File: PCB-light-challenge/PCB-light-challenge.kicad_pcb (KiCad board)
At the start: 2 copper layers, 79.9 x 79 mm, 39 parts, among them J1 Screw_Terminal_01x03, J2 Conn_01x04_Socket, J3 Conn_01x18_Socket, J4 Conn_01x12_Socket, U2 AP9101CK, U3 SP8K32FRATB

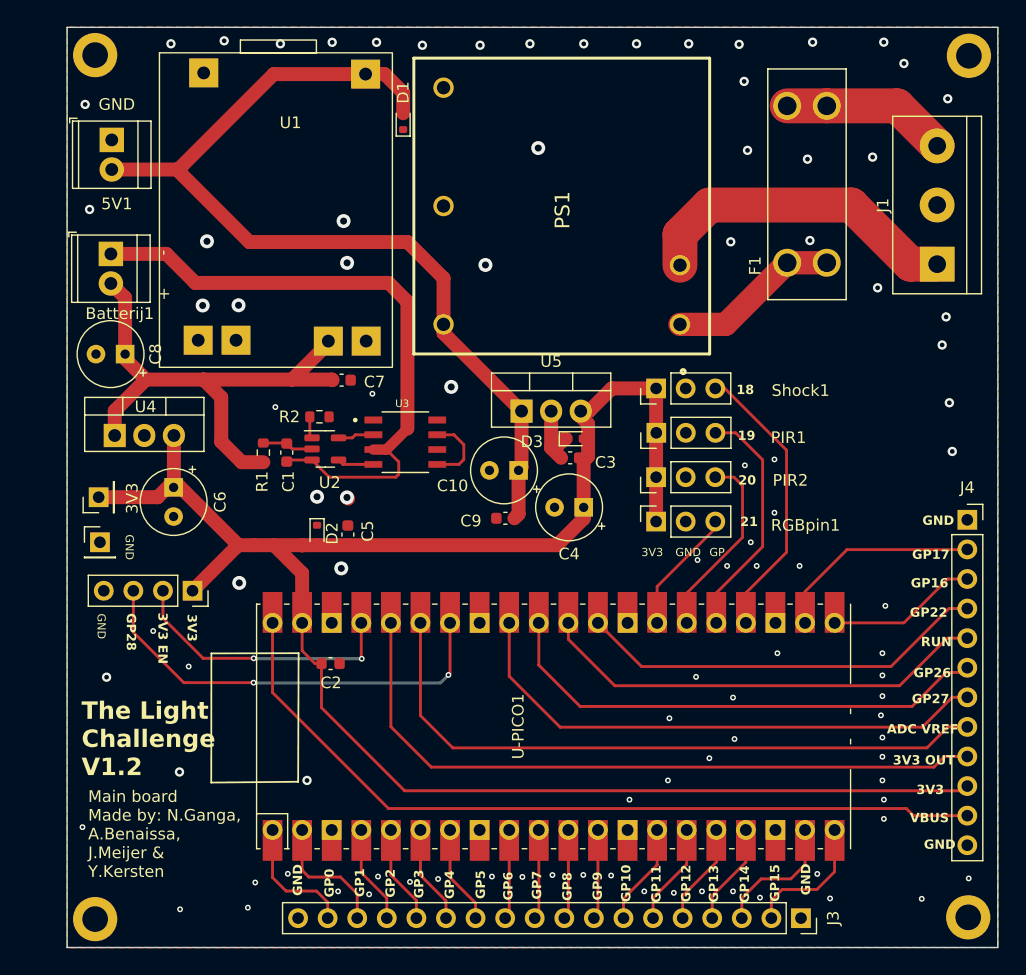
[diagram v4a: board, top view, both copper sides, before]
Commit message: 3V3 OUT voor RGB toegevoegd en footprint van connectoren verandert naar JST
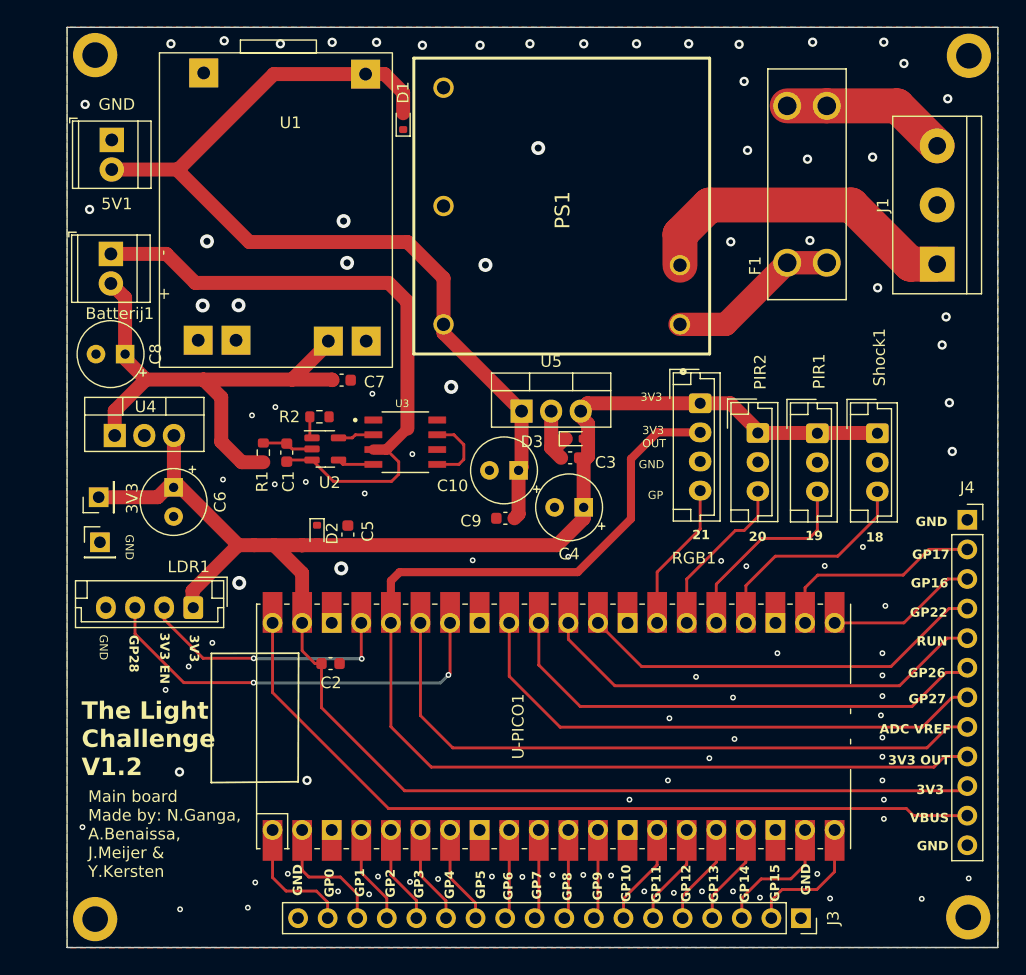
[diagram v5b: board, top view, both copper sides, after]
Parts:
- removed RGBpin1: Conn_01x03_Socket, Connector_PinSocket_2.54mm:PinSocket_1x03_P2.54mm_Vertical
- added RGB1: RGB, Connector_JST:JST_EH_B4B-EH-A_1x04_P2.50mm_Vertical, F.Cu at (226.8, 105.4)
- LDR1: renamed from J2; value Conn_01x04_Socket -> LDR; footprint Connector_PinSocket_2.54mm:PinSocket_1x04_P2.54mm_Vertical -> Connector_JST:JST_EH_B4B-EH-A_1x04_P2.50mm_Vertical
- PIR1, PIR2, Shock1: footprint Connector_PinHeader_2.54mm:PinHeader_1x03_P2.54mm_Vertical -> Connector_JST:JST_EH_B3B-EH-A_1x03_P2.50mm_Vertical
- moved Shock1 19.4 mm to (242.0, 108.0), turned to -90 degrees
- moved PIR1 13.8 mm to (236.9, 108.0), turned to -90 degrees
- moved PIR2 9.53 mm to (231.7, 108.0), turned to -90 degrees
- moved LDR1 1.45 mm to (183.3, 123.0), turned to 180 degrees
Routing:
- net 3V3 OUT: track 60.2 -> 98.7 mm
- net 3V3: track 159.1 -> 168.9 mm
- net GP18: track 24.6 -> 19.1 mm
- net GP19: track 20.7 -> 17.2 mm
- net GP20: track 16.4 -> 14.3 mm
- net GP21: track 10.8 -> 12.9 mm
- net GP28: track 37.2 -> 35.7 mm
- net 3V3 EN: track 24.1 -> 22.6 mm
- net P-: track 6.48 -> 6.34 mm, vias 98 -> 100

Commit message: LDR connector, silkscreen AC,  Mounting hole main pcb aangepast
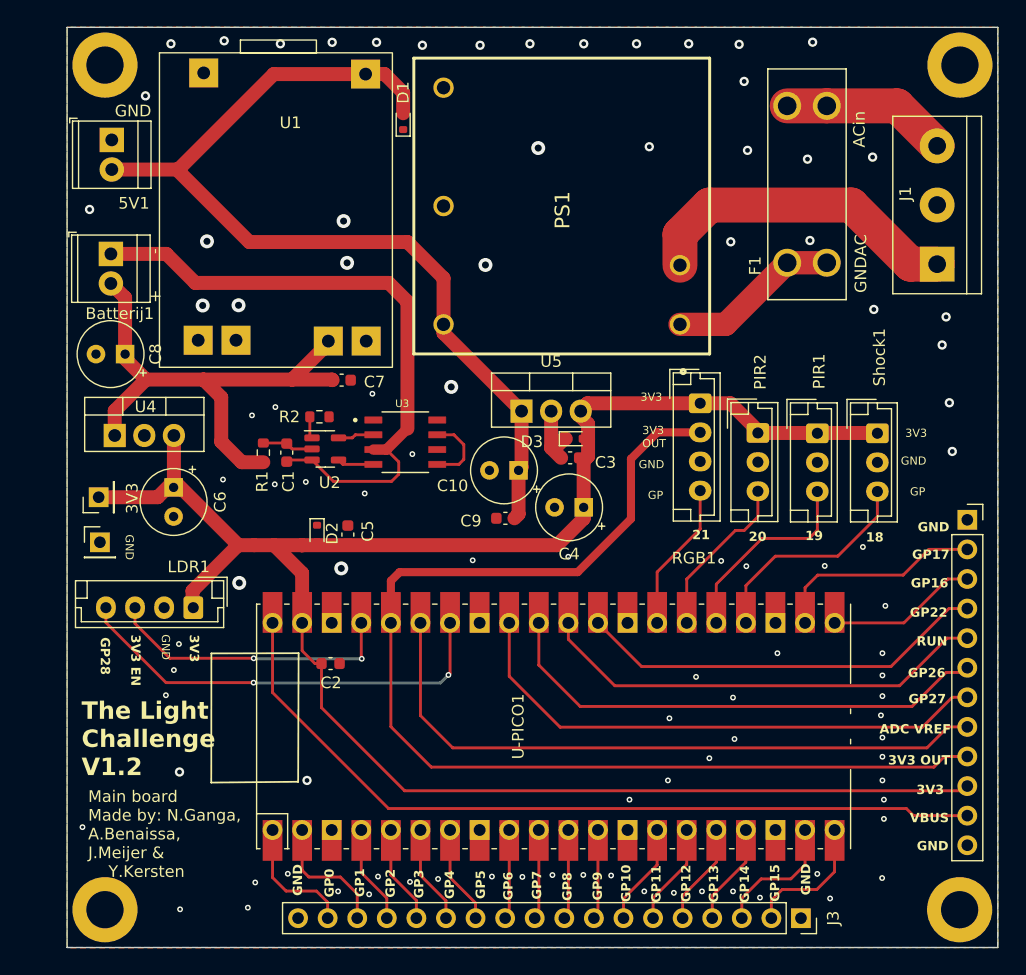
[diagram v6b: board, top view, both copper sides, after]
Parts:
- H1, H2, H3, H4: footprint MountingHole:MountingHole_2.2mm_M2_DIN965_Pad -> MountingHole:MountingHole_3.2mm_M3_DIN965_Pad
- moved H2 1.20 mm to (175.7, 76.4)
- moved H1 1.16 mm to (175.7, 148.9)
- moved H3 1.11 mm to (249.1, 76.4)
- moved H4 0.99 mm to (249.1, 148.9)
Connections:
- LDR1 pad 2: 3V3 EN -> P-
- LDR1 pad 3: GP28 -> 3V3 EN
- LDR1 pad 4: P- -> GP28
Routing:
- net 3V3 EN: track 22.6 -> 25.3 mm
- net GP28: track 35.7 -> 37.6 mm
- net P-: vias 100 -> 97
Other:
- board text added: "ACin"
- board text added: "GNDAC"

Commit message: AC (L) en (N)  weer nagekeken en aangepast
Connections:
- PS1 pad 1: /Battery_charger/Fuse -> /Battery_charger/GNDAC
- PS1 pad 2: /Battery_charger/GNDAC -> /Battery_charger/Fuse
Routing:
- net /Battery_charger/GNDAC: track 27.9 -> 25.1 mm
- net /Battery_charger/Fuse: track 14.8 -> 12.7 mm
- net P-: vias 97 -> 96
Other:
- board text added: "AC(L)"
- board text added: "AC(N)"
- board text removed: "ACin"
- board text removed: "GNDAC"
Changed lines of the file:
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@@
       (stroke (width 0.254) (type solid)) (layer "F.Fab"))
     (pad "1" thru_hole circle (at -10.16 10.15 90) (size 1.75 1.75) (drill 1.15) (layers "*.Cu" "*.Mask")
-      (net 41 "/Battery_charger/Fuse") (pinfunction "AC(N)") (pintype "passive"))
+      (net 43 "/Battery_charger/GNDAC") (pinfunction "AC(N)") (pintype "passive"))
     (pad "2" thru_hole circle (at -5.08 10.15 90) (size 1.75 1.75) (drill 1.15) (layers "*.Cu" "*.Mask")
-      (net 43 "/Battery_charger/GNDAC") (pinfunction "AC(L)") (pintype "passive"))
+      (net 41 "/Battery_charger/Fuse") (pinfunction "AC(L)") (pintype "passive"))
     (pad "3" thru_hole circle (at 10.16 -10.15 90) (size 1.75 1.75) (drill 1.15) (layers "*.Cu" "*.Mask")
       (net 42 "unconnected-(PS1-NC-Pad3)") (pinfunction "NC") (pintype "no_connect"))
@@
     (effects (font (size 0.8 0.8) (thickness 0.15) bold) (justify left bottom))
   )
-  (gr_text "GNDAC" (at 240.5888 93.4212 90) (layer "F.SilkS")
+  (gr_text "AC(N)" (at 240.5888 93.4212 90) (layer "F.SilkS")
     (effects (font (size 1 1) (thickness 0.15)))
   )
-  (gr_text "ACin" (at 240.4618 81.8896 90) (layer "F.SilkS")
+  (gr_text "AC(L)" (at 240.4618 81.8896 90) (layer "F.SilkS")
     (effects (font (size 1 1) (thickness 0.15)))
   )
@@
   (segment (start 206.502 108.966) (end 206.502 110.236) (width 0.25) (layer "F.Cu") (net 39))
   (segment (start 234.266 79.879) (end 237.666 79.879) (width 3) (layer "F.Cu") (net 40))
-  (segment (start 237.666 79.879) (end 243.709 79.879) (width 3) (layer "F.Cu") (net 40))
-  (segment (start 243.709 79.879) (end 247.142 83.312) (width 3) (layer "F.Cu") (net 40))
-  (segment (start 225.06 98.64) (end 228.975 98.64) (width 2) (layer "F.Cu") (net 41))
-  (segment (start 234.266 93.349) (end 237.666 93.349) (width 2) (layer "F.Cu") (net 41))
-  (segment (start 228.975 98.64) (end 234.266 93.349) (width 2) (layer "F.Cu") (net 41))
-  (segment (start 225.06 90.916) (end 225.06 93.56) (width 3) (layer "F.Cu") (net 43))
-  (segment (start 244.856 93.472) (end 239.776 88.392) (width 3) (layer "F.Cu") (net 43))
-  (segment (start 239.776 88.392) (end 227.584 88.392) (width 3) (layer "F.Cu") (net 43))
-  (segment (start 247.142 93.472) (end 244.856 93.472) (width 3) (layer "F.Cu") (net 43))
-  (segment (start 227.584 88.392) (end 225.06 90.916) (width 3) (layer "F.Cu") (net 43))
+  (segment (start 247.142 83.312) (end 243.709 79.879) (width 3) (layer "F.Cu") (net 40))
+  (segment (start 243.709 79.879) (end 237.666 79.879) (width 3) (layer "F.Cu") (net 40))
+  (segment (start 237.666 93.349) (end 234.266 93.349) (width 2) (layer "F.Cu") (net 41))
+  (segment (start 234.055 93.56) (end 234.266 93.349) (width 2) (layer "F.Cu") (net 41))
+  (segment (start 225.06 93.56) (end 234.055 93.56) (width 2) (layer "F.Cu") (net 41))
+  (segment (start 247.142 93.472) (end 240.919 99.695) (width 3) (layer "F.Cu") (net 43))
+  (segment (start 240.919 99.695) (end 226.115 99.695) (width 3) (layer "F.Cu") (net 43))
+  (segment (start 226.115 99.695) (end 225.06 98.64) (width 3) (layer "F.Cu") (net 43))
   (segment (start 214 109.242) (end 214.858 110.1) (width 1.2) (layer "F.Cu") (net 44))
   (segment (start 214 106.09) (end 214 109.242) (width 1.2) (layer "F.Cu") (net 44))
@@
   (via (at 224.155 132.461) (size 0.5) (drill 0.25) (layers "F.Cu" "B.Cu") (free) (net 44))
   (via (at 242.443 134.112) (size 0.5) (drill 0.25) (layers "F.Cu" "B.Cu") (free) (net 44))
-  (via (at 241.7064 97.3582) (size 0.8) (drill 0.4) (layers "F.Cu" "B.Cu") (free) (net 44))
   (via (at 247.91 98) (size 0.8) (drill 0.4) (layers "F.Cu" "B.Cu") (free) (net 44))
   (via (at 236.22 91.44) (size 0.8) (drill 0.4) (layers "F.Cu" "B.Cu") (free) (net 44))

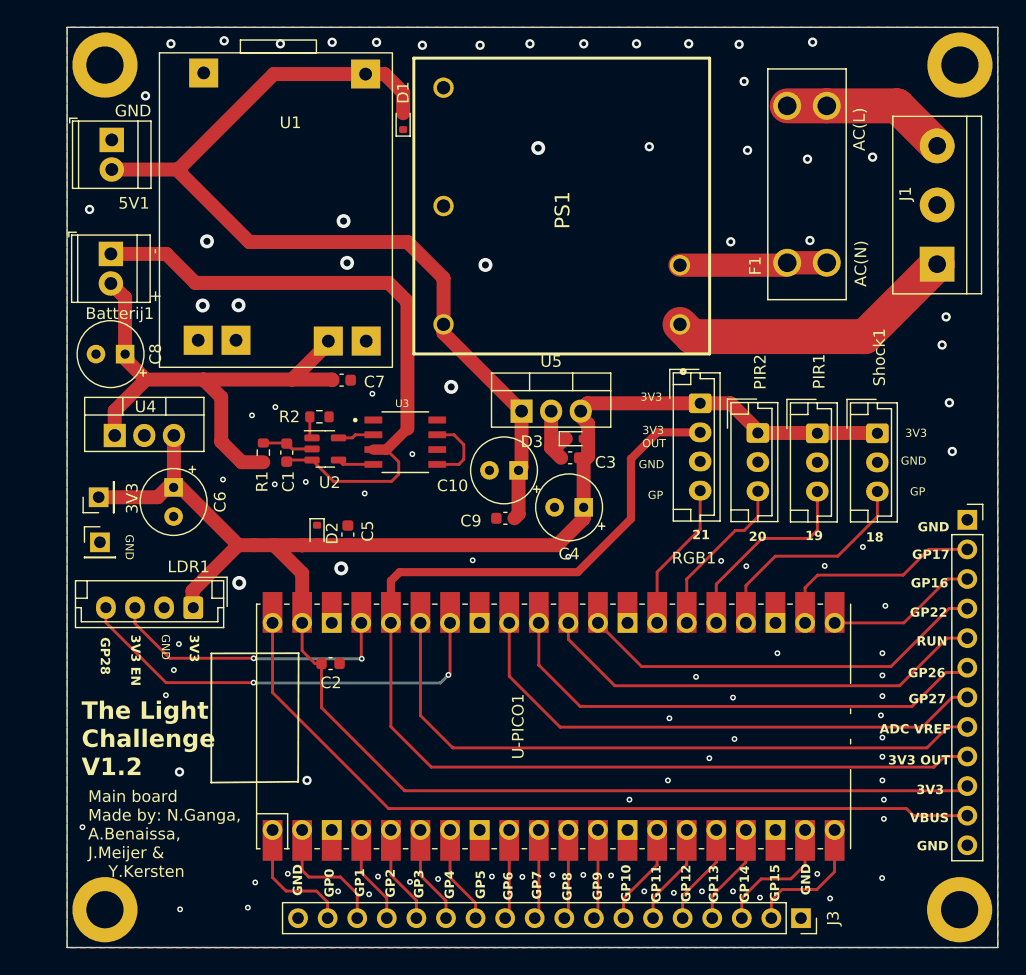
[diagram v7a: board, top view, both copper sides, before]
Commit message: Footprint charger aangepast, connectoren verder van elkaar geplaatst.
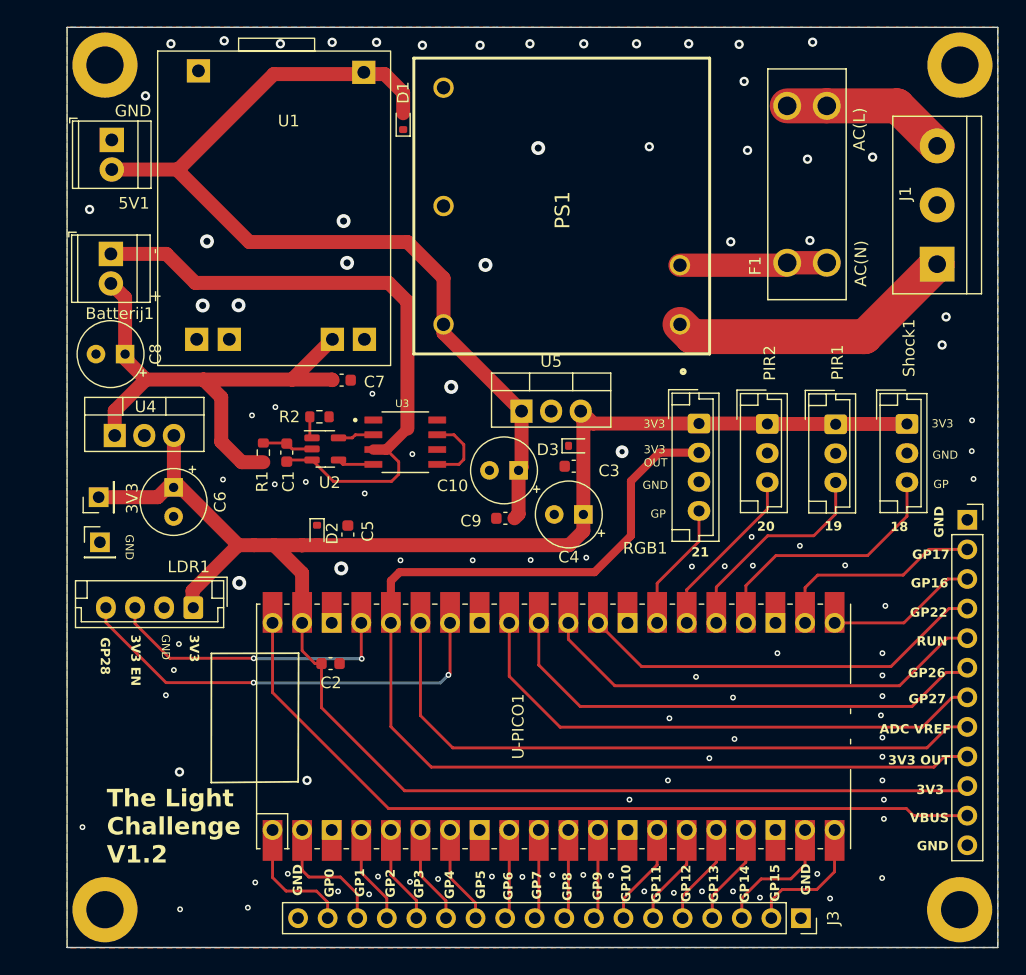
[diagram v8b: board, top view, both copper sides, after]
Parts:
- moved Shock1 2.66 mm to (244.6, 107.2)
- moved PIR1 1.75 mm to (238.4, 107.2)
- moved RGB1 1.74 mm to (226.7, 107.2)
- moved PIR2 1.12 mm to (232.6, 107.2)
- moved C3 0.78 mm to (215.9, 110.8)
- moved D3 0.65 mm to (216.2, 109.1)
- moved C4 0.61 mm to (216.8, 115.0)
- moved U1 0.22 mm to (177.0, 77.9)
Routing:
- net P-: track 6.34 -> 0.39 mm, vias 96 -> 102
- net GP18: track 19.1 -> 22.4 mm
- net 3V3: track 168.9 -> 172.0 mm
- net GP21: track 12.9 -> 11.1 mm
- net GP19: track 17.2 -> 18.6 mm
- net 3V3 OUT: track 98.7 -> 97.6 mm
- net GP20: track 14.3 -> 14.9 mm
